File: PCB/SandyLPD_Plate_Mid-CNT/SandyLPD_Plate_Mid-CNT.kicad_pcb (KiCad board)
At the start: 2 copper layers, 49.4 x 61 mm, 10 parts

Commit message: ゴムシート貼り付けめやすを追加
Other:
- board text added: "Top基板うら側のソケットを逃すように調整。"
- board text removed: "Top基板うら側のソケットを逃すようにを調整。"
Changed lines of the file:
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@@
 		)
 	)
-	(gr_text "Top基板うら側のソケットを逃すようにを調整。"
+	(gr_rect
+		(start 136.483435 76.20028)
+		(end 139.783435 80.20028)
+		(stroke
+			(width 0.1)
+			(type default)
+		)
+		(fill none)
+		(layer "Eco1.User")
+	)
+	(gr_rect
+		(start 133.811653 36.886219)
+		(end 148.811653 41.886219)
+		(stroke
+			(width 0.1)
+			(type default)
+		)
+		(fill none)
+		(layer "Eco1.User")
+	)
+	(gr_rect
+		(start 124.083435 44.30028)
+		(end 129.083435 49.30028)
+		(stroke
+			(width 0.1)
+			(type default)
+		)
+		(fill none)
+		(layer "Eco1.User")
+	)
+	(gr_rect
+		(start 152.833435 89.90028)
+		(end 156.133435 95.90028)
+		(stroke
+			(width 0.1)
+			(type default)
+		)
+		(fill none)
+		(layer "Eco1.User")
+	)
+	(gr_rect
+		(start 119.880385 36.528402)
+		(end 124.880385 41.528402)
+		(stroke
+			(width 0.1)
+			(type default)
+		)
+		(fill none)
+		(layer "Eco1.User")
+	)
+	(gr_rect
+		(start 145.383435 44.80028)
+		(end 150.383435 79.80028)
+		(stroke
+			(width 0.1)
+			(type default)
+		)
+		(fill none)
+		(layer "Eco1.User")
+	)
+	(gr_text "Top基板うら側のソケットを逃すように調整。"
 		(at 109.760068 32.956526 0)
 		(layer "Eco1.User")

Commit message: シルク調整
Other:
- board text removed: "Top基板うら側のソケットを逃すように調整。"
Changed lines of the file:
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@@
 		(layer "Eco1.User")
-	)
-	(gr_text "Top基板うら側のソケットを逃すように調整。"
-		(at 109.760068 32.956526 0)
-		(layer "Eco1.User")
-		(effects
-			(font
-				(size 3 3)
-				(thickness 0.3)
-			)
-			(justify left bottom)
-		)
 	)
 	(zone

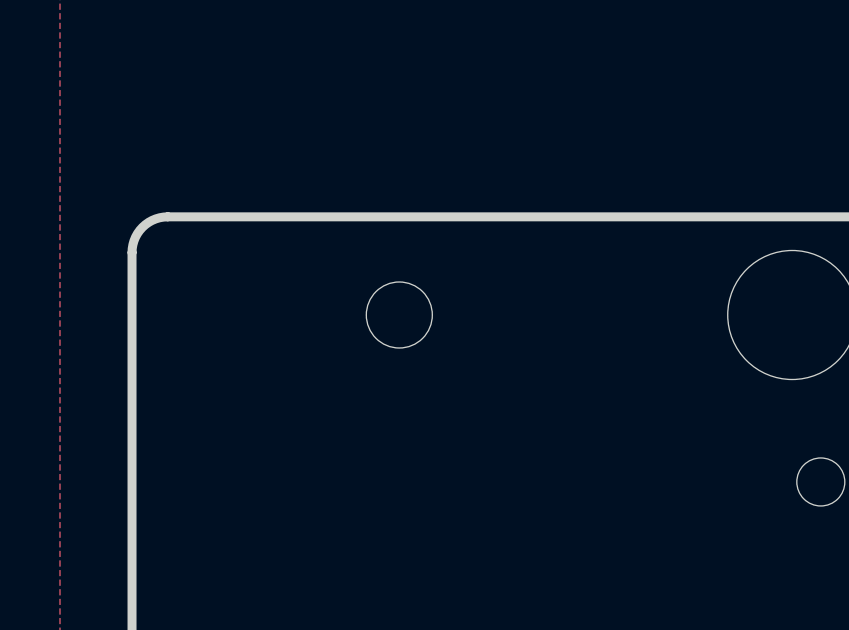
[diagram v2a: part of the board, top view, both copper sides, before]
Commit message: Mid-CNTのプレート固定用スルーホールタップを1個減らす
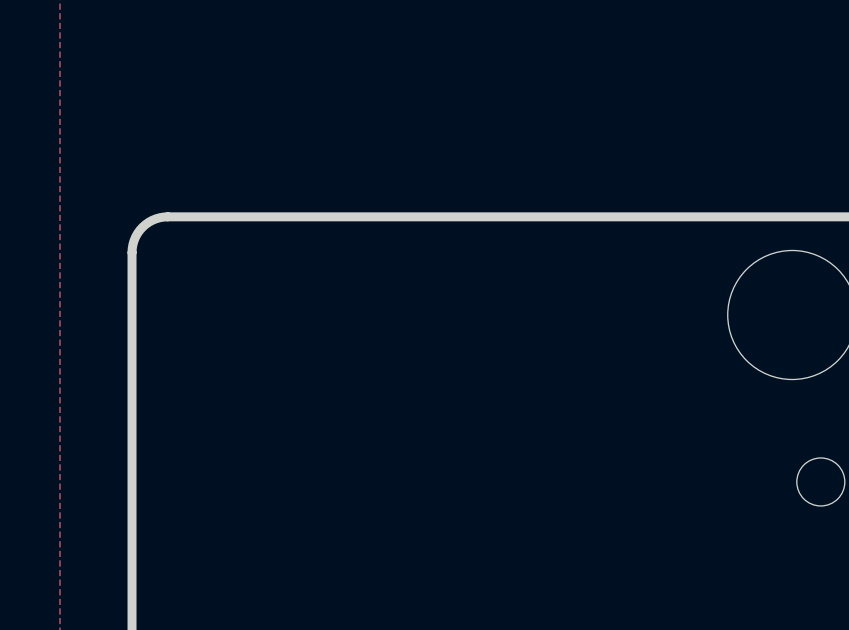
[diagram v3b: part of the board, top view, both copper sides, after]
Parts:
- removed the H5 at (116.3, 38.9)
- renumbered H6 to H5
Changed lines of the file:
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@@
 	(footprint "MountingHole:MountingHole_2.2mm_M2"
 		(layer "F.Cu")
-		(at 116.308435 38.909656)
+		(at 153.81323 68.70032)
 		(descr "Mounting Hole 2.2mm, no annular, M2")
 		(tags "mounting hole 2.2mm no annular m2")
@@
 			(at 0 -3.2 0)
 			(layer "F.SilkS")
-			(hide yes)
-			(effects
-				(font
-					(size 1 1)
-					(thickness 0.15)
-				)
-			)
-		)
-		(property "Value" "MountingHole"
-			(at 0 3.2 0)
-			(layer "F.Fab")
-			(effects
-				(font
-					(size 1 1)
-					(thickness 0.15)
-				)
-			)
-		)
-		(property "Footprint" "MountingHole:MountingHole_2.2mm_M2"
-			(at 0 0 0)
-			(unlocked yes)
-			(layer "F.Fab")
-			(hide yes)
-			(effects
-				(font
-					(size 1.27 1.27)
-					(thickness 0.15)
-				)
-			)
-		)
-		(property "Datasheet" ""
-			(at 0 0 0)
-			(unlocked yes)
-			(layer "F.Fab")
-			(hide yes)
-			(effects
-				(font
-					(size 1.27 1.27)
-					(thickness 0.15)
-				)
-			)
-		)
-		(property "Description" "Mounting Hole without connection"
-			(at 0 0 0)
-			(unlocked yes)
-			(layer "F.Fab")
-			(hide yes)
-			(effects
-				(font
-					(size 1.27 1.27)
-					(thickness 0.15)
-				)
-			)
-		)
-		(property ki_fp_filters "MountingHole*")
-		(sheetname "ルート")
-		(sheetfile "SandyLPD_Plate_Mid-CNT.kicad_sch")
-		(attr exclude_from_pos_files exclude_from_bom)
-		(fp_circle
-			(center 0 0)
-			(end 2.2 0)
-			(stroke
-				(width 0.15)
-				(type solid)
-			)
-			(fill none)
-			(layer "Cmts.User")
-		)
-		(fp_circle
-			(center 0 0)
-			(end 2.45 0)
-			(stroke
-				(width 0.05)
-				(type solid)
-			)
-			(fill none)
-			(layer "F.CrtYd")
-		)
-		(fp_text user "${REFERENCE}"
-			(at 0 0 0)
-			(layer "F.Fab")
-			(effects
-				(font
-					(size 1 1)
-					(thickness 0.15)
-				)
-			)
-		)
-		(pad "" np_thru_hole circle
-			(at 0 0)
-			(size 2.2 2.2)
-			(drill 2.2)
-			(layers "*.Cu" "*.Mask")
-		)
-		(model "${KIPRJMOD}/locallib.pretty/M2 x 3 Screw head.STEP"
-			(offset
-				(xyz 0 0 1.6)
-			)
-			(scale
-				(xyz 1 1 1)
-			)
-			(rotate
-				(xyz 0 -90 0)
-			)
-		)
-	)
-	(footprint "MountingHole:MountingHole_2.2mm_M2"
-		(layer "F.Cu")
-		(at 153.81323 68.70032)
-		(descr "Mounting Hole 2.2mm, no annular, M2")
-		(tags "mounting hole 2.2mm no annular m2")
-		(property "Reference" "H6"
-			(at 0 -3.2 0)
-			(layer "F.SilkS")
